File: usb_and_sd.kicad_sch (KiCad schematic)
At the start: 72 parts, among them J6001 USB_C_Receptacle_USB2.0_16P, J6002 USB_A, J6003 Micro_SD_Card_Det1, U1002 AM6231ASGGGAALW, U6001 TVS0500DRVR, U6002 KLMAG2GEUF-B04P, U6003 TPD3S014, U6004 TPS22918DBVR

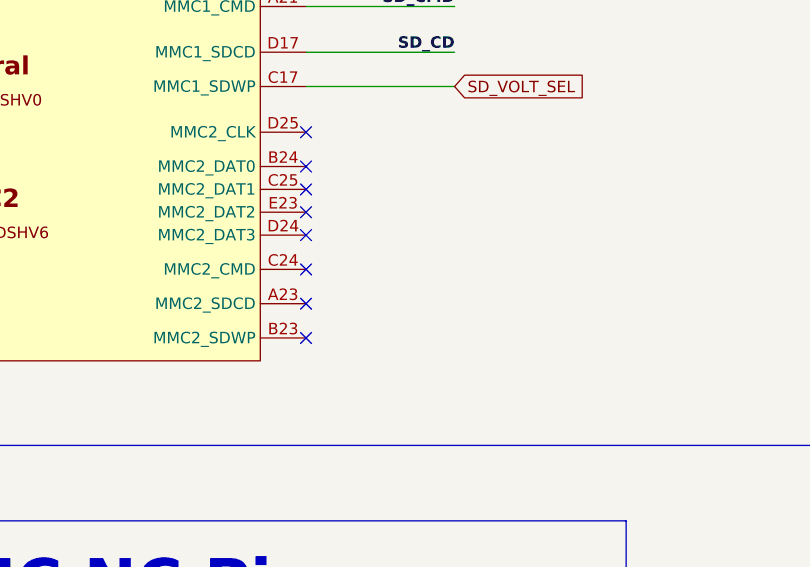
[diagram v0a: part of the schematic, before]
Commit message: Added status LEDs for SoC power, MGM240P power, and for GPIO0_70
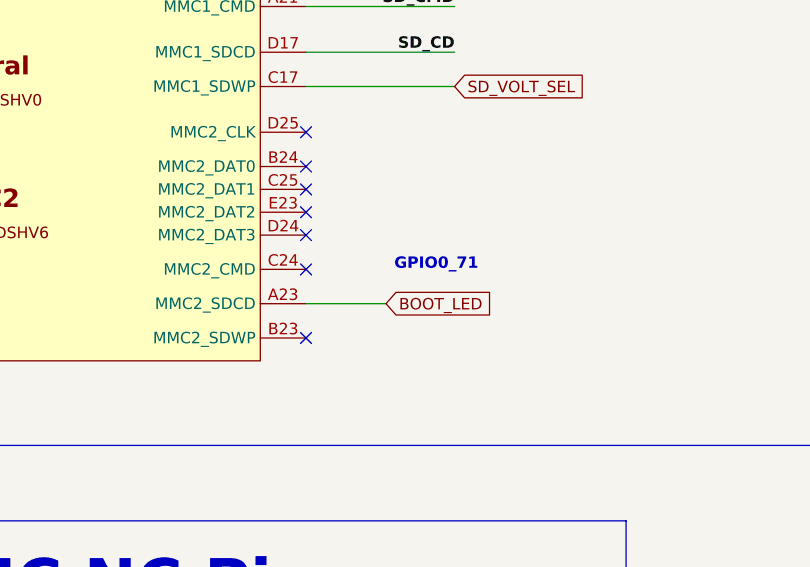
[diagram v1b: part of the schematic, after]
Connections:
- net BOOT_LED: now reaches U1002.A23 (MMC2_SDCD)
- no-connect marks 15 -> 14
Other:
- note added: "GPIO0_71"
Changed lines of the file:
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@@
 		)
 	)
+	(text "GPIO0_71"
+		(exclude_from_sim no)
+		(at 405.638 193.802 0)
+		(effects
+			(font
+				(size 1.27 1.27)
+				(thickness 0.254)
+				(bold yes)
+			)
+		)
+	)
 	(text "RB520S30T1G"
 		(exclude_from_sim no)
@@
 	)
 	(no_connect
-		(at 391.16 198.12)
-	)
-	(no_connect
 		(at 101.6 182.88)
 	)
@@
 	(wire
 		(pts
+			(xy 391.16 198.12) (xy 400.05 198.12)
+		)
+		(stroke
+			(width 0)
+			(type default)
+		)
+	)
+	(wire
+		(pts
 			(xy 520.7 134.62) (xy 530.86 134.62)
 		)
@@
 				(hide yes)
 			)
+		)
+	)
+	(global_label "BOOT_LED"
+		(shape input)
+		(at 400.05 198.12 0)
+		(fields_autoplaced yes)
+		(effects
+			(font
+				(size 1.27 1.27)
+			)
+			(justify left)
+		)
+		(property "Intersheetrefs" "${INTERSHEET_REFS}"
+			(at 412.3485 198.12 0)
+			(effects
+				(font
+					(size 1.27 1.27)
+				)
+				(justify left)
+				(hide yes)
+			)

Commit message: Added JLCPCB part numbers for some caps
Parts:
- C6001, C6005: JLCPCB Part# (none) -> C106859
- C6003, C6007, C6008, C6011, C6015: JLCPCB Part# (none) -> C60474
- C6004, C6014: JLCPCB Part# (none) -> C106254
- C6006, C6010: JLCPCB Part# (none) -> C19702
- C6009: JLCPCB Part# (none) -> C326606

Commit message: All capacitors and crystals added to BOM. 150u cap for USB A changed to tantalum and rerouted
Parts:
- removed C6012: 150u, Capacitor_SMD:C_1206_3216Metric, symbol Device:C
- added C6012: 150u, Capacitor_Tantalum_SMD:CP_EIA-7343-31_Kemet-D, symbol Device:C_Polarized
- C6002: JLCPCB Part# (none) -> C326836
- C6013: JLCPCB Part# (none) -> C1705
- C6016, C6017: JLCPCB Part# (none) -> C784585
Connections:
- net GND: now also C6012.2
- net USB_A_VBUS: now also C6012.1
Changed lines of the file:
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@@
 	)
 	(symbol
+		(lib_id "Device:C_Polarized")
+		(at 231.14 260.35 0)
+		(unit 1)
+		(exclude_from_sim no)
+		(in_bom yes)
+		(on_board yes)
+		(dnp no)
+		(fields_autoplaced yes)
+		(property "Reference" "C6012"
+			(at 234.95 258.1909 0)
+			(effects
+				(font
+					(size 1.27 1.27)
+				)
+				(justify left)
+			)
+		)
+		(property "Value" "150u"
+			(at 234.95 260.7309 0)
+			(effects
+				(font
+					(size 1.27 1.27)
+				)
+				(justify left)
+			)
+		)
+		(property "Footprint" "Capacitor_Tantalum_SMD:CP_EIA-7343-31_Kemet-D"
+			(at 232.1052 264.16 0)
+			(effects
+				(font
+					(size 1.27 1.27)
+				)
+				(hide yes)
+			)
+		)
+		(property "Datasheet" "~"
+			(at 231.14 260.35 0)
+			(effects
+				(font
+					(size 1.27 1.27)
+				)
+				(hide yes)
+			)
+		)
+		(property "Description" "Polarized capacitor"
+			(at 231.14 260.35 0)
+			(effects
+				(font
+					(size 1.27 1.27)
+				)
+				(hide yes)
+			)
+		)
+		(property "JLCPCB Part#" "C122324"
+			(at 231.14 260.35 0)
+			(effects
+				(font
+					(size 1.27 1.27)
+				)
+			)
+		)
+		(pin "1"
+		)
+		(pin "2"
+		)
+		(instances
+			(project ""
+				(path "/b43b7bca-e50d-42ec-8ff0-e0016dfefe0a/e2459660-886d-4599-a9e6-b9bb7931d0e6"
+					(reference "C6012")
+					(unit 1)
+				)
+			)
+		)
+	)
+	(symbol
 		(lib_id "Device:C")
 		(at 586.74 318.77 0)
@@
 			)
 		)
-		(property "JLCPCB Part#" ""
+		(property "JLCPCB Part#" "C784585"
 			(at 615.95 387.35 0)
 			(effects
@@
 			)
 		)
-		(property "JLCPCB Part#" ""
+		(property "JLCPCB Part#" "C326836"
 			(at 594.36 116.84 0)
 			(effects
@@
 			)
 		)
-		(property "JLCPCB Part#" ""
+		(property "JLCPCB Part#" "C784585"
 			(at 576.58 387.35 0)
 			(effects
@@
 			)
 		)
-		(property "JLCPCB Part#" ""
+		(property "JLCPCB Part#" " C1705"
 			(at 599.44 318.77 0)
 			(effects
@@
 					(unit 1)
 				)
-			)
-		)
-	)
-	(symbol
-		(lib_id "Device:C")
-		(at 231.14 260.35 0)
-		(unit 1)
-		(exclude_from_sim no)
-		(in_bom yes)
-		(on_board yes)
-		(dnp no)
-		(fields_autoplaced yes)
-		(property "Reference" "C6012"
-			(at 234.95 259.0799 0)
-			(effects
-				(font
-					(size 1.27 1.27)
-				)
-				(justify left)
-			)
-		)
-		(property "Value" "150u"
-			(at 234.95 261.6199 0)
-			(effects
-				(font
-					(size 1.27 1.27)
-				)
-				(justify left)
-			)
-		)
-		(property "Footprint" "Capacitor_SMD:C_1206_3216Metric"
-			(at 232.1052 264.16 0)
-			(effects
-				(font
-					(size 1.27 1.27)
-				)
-				(hide yes)
-			)
-		)
-		(property "Datasheet" "~"
-			(at 231.14 260.35 0)
-			(effects
-				(font
-					(size 1.27 1.27)
-				)
-				(hide yes)
-			)
-		)
-		(property "Description" "Unpolarized capacitor"
-			(at 231.14 260.35 0)
-			(effects
-				(font
-					(size 1.27 1.27)
-				)
-				(hide yes)
-			)
-		)
-		(property "JLCPCB Part#" ""
-			(at 231.14 260.35 0)
-			(effects
-				(font
-					(size 1.27 1.27)
-				)
-			)
-		)
-		(pin "1"
-		)
-		(pin "2"
-		)
-		(instances
-			(project "Leonhart"
-				(path "/b43b7bca-e50d-42ec-8ff0-e0016dfefe0a/e2459660-886d-4599-a9e6-b9bb7931d0e6"
-					(reference "C6012")
-					(unit 1)
-				)

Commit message: Added diode and tvs diode JLC part numbers to BOM. Also fixed tvs diode footprint
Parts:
- D6001, D6002, D6006, D6007, D6008, D6009, D6010, D6011, D6012: JLCPCB Part# (none) -> C779408
- D6003, D6004, D6005, D6013, D6014: JLCPCB Part# (none) -> C154821
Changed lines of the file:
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@@
 			)
 		)
-		(property "JLCPCB Part#" ""
+		(property "JLCPCB Part#" "C154821"
 			(at 548.64 378.46 0)
 			(effects
@@
 			)
 		)
-		(property "JLCPCB Part#" ""
+		(property "JLCPCB Part#" "C779408"
 			(at 201.93 161.29 0)
 			(effects
@@
 			)
 		)
-		(property "JLCPCB Part#" ""
+		(property "JLCPCB Part#" "C154821"
 			(at 520.7 200.66 0)
 			(effects
@@
 			)
 		)
-		(property "JLCPCB Part#" ""
+		(property "JLCPCB Part#" "C154821"
 			(at 520.7 195.58 0)
 			(effects
@@
 			)
 		)
-		(property "JLCPCB Part#" ""
+		(property "JLCPCB Part#" "C779408"
 			(at 561.34 318.77 0)
 			(effects
@@
 			)
 		)
-		(property "JLCPCB Part#" ""
+		(property "JLCPCB Part#" "C779408"
 			(at 530.86 318.77 0)
 			(effects
@@
 			)
 		)
-		(property "JLCPCB Part#" ""
+		(property "JLCPCB Part#" "C779408"
 			(at 190.5 161.29 0)
 			(effects
@@
 			)
 		)
-		(property "JLCPCB Part#" ""
+		(property "JLCPCB Part#" "C779408"
 			(at 623.57 321.31 0)
 			(effects
@@
 			)
 		)
-		(property "JLCPCB Part#" ""
+		(property "JLCPCB Part#" "C779408"
 			(at 551.18 318.77 0)
 			(effects
@@
 			)
 		)
-		(property "JLCPCB Part#" ""
+		(property "JLCPCB Part#" "C779408"
 			(at 541.02 318.77 0)
 			(effects
@@
 			)
 		)
-		(property "JLCPCB Part#" ""
+		(property "JLCPCB Part#" "C779408"
 			(at 520.7 318.77 0)
 			(effects
@@
 			)
 		)
-		(property "JLCPCB Part#" ""
+		(property "JLCPCB Part#" "C154821"
 			(at 520.7 205.74 0)
 			(effects
@@
 			)
 		)
-		(property "JLCPCB Part#" ""
+		(property "JLCPCB Part#" "C779408"
 			(at 510.54 318.77 0)
 			(effects
@@
 			)
 		)
-		(property "JLCPCB Part#" ""
+		(property "JLCPCB Part#" "C154821"
 			(at 548.64 383.54 0)
 			(effects

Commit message: All JLC part numbers added to BOM except LEDs
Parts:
- J6001: JLCPCB Part# (none) -> C165948
- J6002: JLCPCB Part# (none) -> C46407
- J6003: JLCPCB Part# (none) -> C7301403
- L6001, L6002: JLCPCB Part# (none) -> C2651125
- R6001: JLCPCB Part# (none) -> C155743
- R6002, R6020, R6022, R6024, R6025, R6026, R6027, R6028, R6029, R6030, R6031: JLCPCB Part# (none) -> C60490
- R6003, R6021: JLCPCB Part# (none) -> C93942
- R6004, R6005, R6006, R6007, R6008, R6009, R6010, R6011, R6012, R6013, R6019: JLCPCB Part# (none) -> C137969
- R6014: JLCPCB Part# (none) -> C114765
- R6015, R6018: JLCPCB Part# (none) -> C137970
- R6016, R6017: JLCPCB Part# (none) -> C105872
- R6023: JLCPCB Part# (none) -> C106235
- U1002: JLCPCB Part# (none) -> C7072556
- U6001: JLCPCB Part# (none) -> C609571
- U6002: JLCPCB Part# (none) -> C2920514
- U6003: JLCPCB Part# (none) -> C87384
- U6004: JLCPCB Part# (none) -> C131941
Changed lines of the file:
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@@
 			)
 		)
-		(property "JLCPCB Part#" ""
+		(property "JLCPCB Part#" "C2651125"
 			(at 181.61 194.31 0)
 			(effects
@@
 			)
 		)
-		(property "JLCPCB Part#" ""
+		(property "JLCPCB Part#" "C137969"
 			(at 500.38 139.7 0)
 			(effects
@@
 			)
 		)
-		(property "JLCPCB Part#" ""
+		(property "JLCPCB Part#" "C2920514"
 			(at 393.7 276.86 0)
 			(effects
@@
 			)
 		)
-		(property "JLCPCB Part#" ""
+		(property "JLCPCB Part#" "C93942"
 			(at 135.89 132.08 0)
 			(effects
@@
 			)
 		)
-		(property "JLCPCB Part#" ""
+		(property "JLCPCB Part#" "C2651125"
 			(at 160.02 147.32 0)
 			(effects
@@
 			)
 		)
-		(property "JLCPCB Part#" ""
+		(property "JLCPCB Part#" "C114765"
 			(at 415.29 149.86 0)
 			(effects
@@
 			)
 		)
-		(property "JLCPCB Part#" ""
+		(property "JLCPCB Part#" "C137969"
 			(at 490.22 139.7 0)
 			(effects
@@
 			)
 		)
-		(property "JLCPCB Part#" ""
+		(property "JLCPCB Part#" "C137969"
 			(at 541.02 139.7 0)
 			(effects
@@
 			)
 		)
-		(property "JLCPCB Part#" ""
+		(property "JLCPCB Part#" "C155743"
 			(at 415.29 119.38 0)
 			(effects
@@
 			)
 		)
-		(property "JLCPCB Part#" ""
+		(property "JLCPCB Part#" "C137969"
 			(at 551.18 139.7 0)
 			(effects
@@
 			)
 		)
-		(property "JLCPCB Part#" ""
+		(property "JLCPCB Part#" "C137969"
 			(at 581.66 139.7 0)
 			(effects
@@
 			)
 		)
-		(property "JLCPCB Part#" ""
+		(property "JLCPCB Part#" "C60490"
 			(at 571.5 198.12 0)
 			(effects
@@
 			)
 		)
-		(property "JLCPCB Part#" ""
+		(property "JLCPCB Part#" "C60490"
 			(at 623.57 284.48 0)
 			(effects
@@
 			)
 		)
-		(property "JLCPCB Part#" ""
+		(property "JLCPCB Part#" "C60490"
 			(at 560.07 370.84 0)
 			(effects
@@
 			)
 		)
-		(property "JLCPCB Part#" ""
+		(property "JLCPCB Part#" "C137970"
 			(at 138.43 161.29 0)
 			(effects
@@
 			)
 		)
-		(property "JLCPCB Part#" ""
+		(property "JLCPCB Part#" "C46407"
 			(at 256.54 194.31 0)
 			(effects
@@
 			)
 		)
-		(property "JLCPCB Part#" ""
+		(property "JLCPCB Part#" "C105872"
 			(at 224.79 161.29 0)
 			(effects
@@
 			)
 		)
-		(property "JLCPCB Part#" ""
+		(property "JLCPCB Part#" "C137970"
 			(at 121.92 172.72 0)
 			(effects
@@
 			)
 		)
-		(property "JLCPCB Part#" ""
+		(property "JLCPCB Part#" "C60490"
 			(at 520.7 284.48 0)
 			(effects
@@
 			)
 		)
-		(property "JLCPCB Part#" ""
+		(property "JLCPCB Part#" "C87384"
 			(at 207.01 248.92 0)
 			(effects
@@
 			)
 		)
-		(property "JLCPCB Part#" ""
+		(property "JLCPCB Part#" "C7072556"
 			(at 358.14 160.02 0)
 			(effects
@@
 			)
 		)
-		(property "JLCPCB Part#" ""
+		(property "JLCPCB Part#" "C137969"
 			(at 561.34 198.12 0)
 			(effects
@@
 			)
 		)
-		(property "JLCPCB Part#" ""
+		(property "JLCPCB Part#" "C60490"
 			(at 510.54 284.48 0)
 			(effects
@@
 			)
 		)
-		(property "JLCPCB Part#" ""
+		(property "JLCPCB Part#" "C165948"
 			(at 257.81 147.32 0)
 			(effects
@@
 			)
 		)
-		(property "JLCPCB Part#" ""
+		(property "JLCPCB Part#" "C609571"
 			(at 182.88 120.65 0)
 			(effects
@@
 			)
 		)
-		(property "JLCPCB Part#" ""
+		(property "JLCPCB Part#" "C137969"
 			(at 530.86 139.7 0)
 			(effects
@@
 			)
 		)
-		(property "JLCPCB Part#" ""
+		(property "JLCPCB Part#" "C60490"
 			(at 143.51 219.71 0)
 			(effects
@@
 			)
 		)
-		(property "JLCPCB Part#" ""
+		(property "JLCPCB Part#" "C131941"
 			(at 598.17 378.46 0)
 			(effects
@@
 			)
 		)
-		(property "JLCPCB Part#" ""
+		(property "JLCPCB Part#" "C137969"
 			(at 571.5 139.7 0)
 			(effects
@@
 			)
 		)
-		(property "JLCPCB Part#" ""
+		(property "JLCPCB Part#" "C137969"
 			(at 520.7 139.7 0)
 			(effects
@@
 			)
 		)
-		(property "JLCPCB Part#" ""
+		(property "JLCPCB Part#" "C2920514"
 			(at 618.49 173.99 0)
 			(effects
@@
 			)
 		)
-		(property "JLCPCB Part#" ""
+		(property "JLCPCB Part#" "C7301403"
 			(at 651.51 302.26 0)
 			(effects
@@
 			)
 		)
-		(property "JLCPCB Part#" ""
+		(property "JLCPCB Part#" "C137969"
 			(at 510.54 139.7 0)
 			(effects
@@
 			)
 		)
-		(property "JLCPCB Part#" ""
+		(property "JLCPCB Part#" "C137969"
 			(at 561.34 139.7 0)
 			(effects
@@
 			)
 		)
-		(property "JLCPCB Part#" ""
+		(property "JLCPCB Part#" "C60490"
 			(at 120.65 132.08 0)
 			(effects
@@
 			)
 		)
-		(property "JLCPCB Part#" ""
+		(property "JLCPCB Part#" "C106235"
 			(at 154.94 251.46 0)
 			(effects
@@
 			)
 		)
-		(property "JLCPCB Part#" ""
+		(property "JLCPCB Part#" "C105872"
 			(at 213.36 161.29 0)
 			(effects
@@
 			)
 		)
-		(property "JLCPCB Part#" ""
+		(property "JLCPCB Part#" "C60490"
 			(at 561.34 284.48 0)
 			(effects
@@
 			)
 		)
-		(property "JLCPCB Part#" ""
+		(property "JLCPCB Part#" "C60490"
 			(at 530.86 284.48 0)
 			(effects
@@
 			)
 		)
-		(property "JLCPCB Part#" ""
+		(property "JLCPCB Part#" "C93942"
 			(at 154.94 212.09 0)
 			(effects
@@
 			)
 		)
-		(property "JLCPCB Part#" ""
+		(property "JLCPCB Part#" "C60490"
 			(at 551.18 284.48 0)
 			(effects
@@
 			)
 		)
-		(property "JLCPCB Part#" ""
+		(property "JLCPCB Part#" "C60490"
 			(at 541.02 284.48 0)
 			(effects
@@
 			)
 		)
-		(property "JLCPCB Part#" ""
+		(property "JLCPCB Part#" "C7072556"
 			(at 73.66 168.91 0)
 			(effects

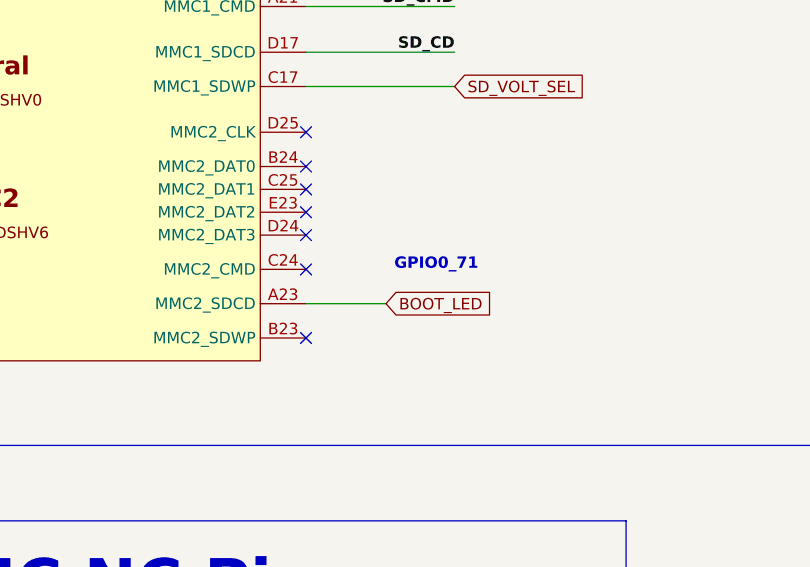
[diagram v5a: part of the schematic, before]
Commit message: Changed ethernet phy strap options and added DNP options for debugging
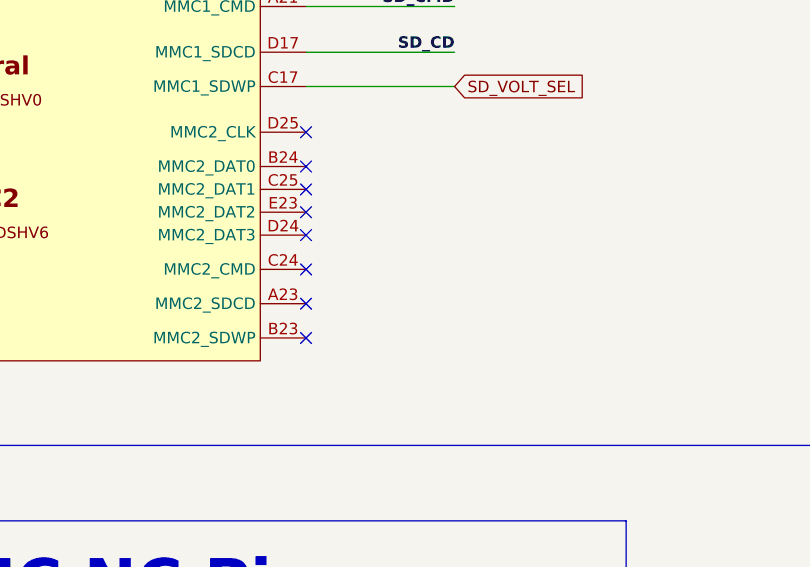
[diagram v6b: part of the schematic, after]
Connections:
- net BOOT_LED: no longer names the net of U1002.A23 (MMC2_SDCD)
- no-connect marks 14 -> 15
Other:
- note removed: "GPIO0_71"
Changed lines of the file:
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@@
 		)
 	)
-	(text "GPIO0_71"
-		(exclude_from_sim no)
-		(at 405.638 193.802 0)
-		(effects
-			(font
-				(size 1.27 1.27)
-				(thickness 0.254)
-				(bold yes)
-			)
-		)
-	)
 	(text "RB520S30T1G"
 		(exclude_from_sim no)
@@
 	)
 	(no_connect
+		(at 391.16 198.12)
+	)
+	(no_connect
 		(at 101.6 182.88)
 	)
@@
 	(wire
 		(pts
-			(xy 391.16 198.12) (xy 400.05 198.12)
-		)
-		(stroke
-			(width 0)
-			(type default)
-		)
-	)
-	(wire
-		(pts
 			(xy 520.7 134.62) (xy 530.86 134.62)
 		)
@@
 				(hide yes)
 			)
-		)
-	)
-	(global_label "BOOT_LED"
-		(shape input)
-		(at 400.05 198.12 0)
-		(fields_autoplaced yes)
-		(effects
-			(font
-				(size 1.27 1.27)
-			)
-			(justify left)
-		)
-		(property "Intersheetrefs" "${INTERSHEET_REFS}"
-			(at 412.3485 198.12 0)
-			(effects
-				(font
-					(size 1.27 1.27)
-				)
-				(justify left)
-				(hide yes)
-			)

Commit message: Ordered Rev A
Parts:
- U6002: value KLMAG2GEUF-B04P -> SDINBDG4-16G; JLCPCB Part# C2920514 -> C2830396
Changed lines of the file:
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@@
 			)
 		)
-		(property "Value" "KLMAG2GEUF-B04P"
+		(property "Value" "SDINBDG4-16G"
 			(at 381 243.84 0)
 			(effects
@@
 			)
 		)
-		(property "JLCPCB Part#" "C2920514"
+		(property "JLCPCB Part#" "C2830396"
 			(at 393.7 276.86 0)
 			(effects
@@
 			)
 		)
-		(property "Value" "KLMAG2GEUF-B04P"
+		(property "Value" "SDINBDG4-16G"
 			(at 655.574 170.18 0)
 			(effects
@@
 			)
 		)
-		(property "JLCPCB Part#" "C2920514"
+		(property "JLCPCB Part#" "C2830396"
 			(at 618.49 173.99 0)
 			(effects

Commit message: Canceled order, fixed microSD socket footprint issue. Fixed eMMC trace width issue
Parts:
- J6003: footprint TF-15x15:TF15X15 -> MEM2052-00-195-00-A:MEM20520019500A
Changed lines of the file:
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@@
 			)
 		)
-		(property "Footprint" "TF-15x15:TF15X15"
+		(property "Footprint" "MEM2052-00-195-00-A:MEM20520019500A"
 			(at 703.58 284.48 0)
 			(effects
